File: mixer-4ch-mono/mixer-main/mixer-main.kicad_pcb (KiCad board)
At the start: 2 copper layers, 35 parts, among them J1 USB_C_Receptacle_PowerOnly_6P, J2 Conn_01x02, J3 Conn_01x02, J4 Conn_01x02, J5 Conn_01x02, J6 Conn_01x02, U1 TLV9062IDR, U2 TLV431AIDBZR, U3 SPX3819M5-L-3-3

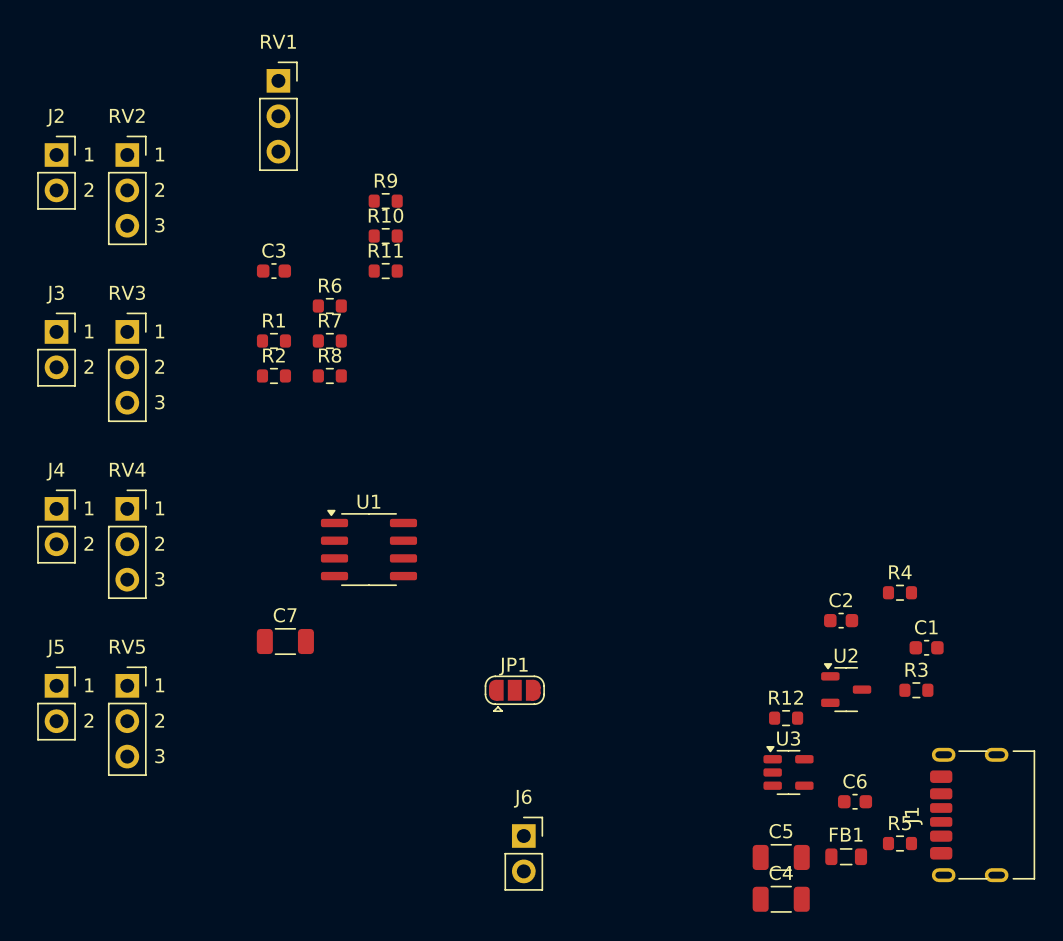
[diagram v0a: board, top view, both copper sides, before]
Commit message: Update mixer-main
Continued with layout.
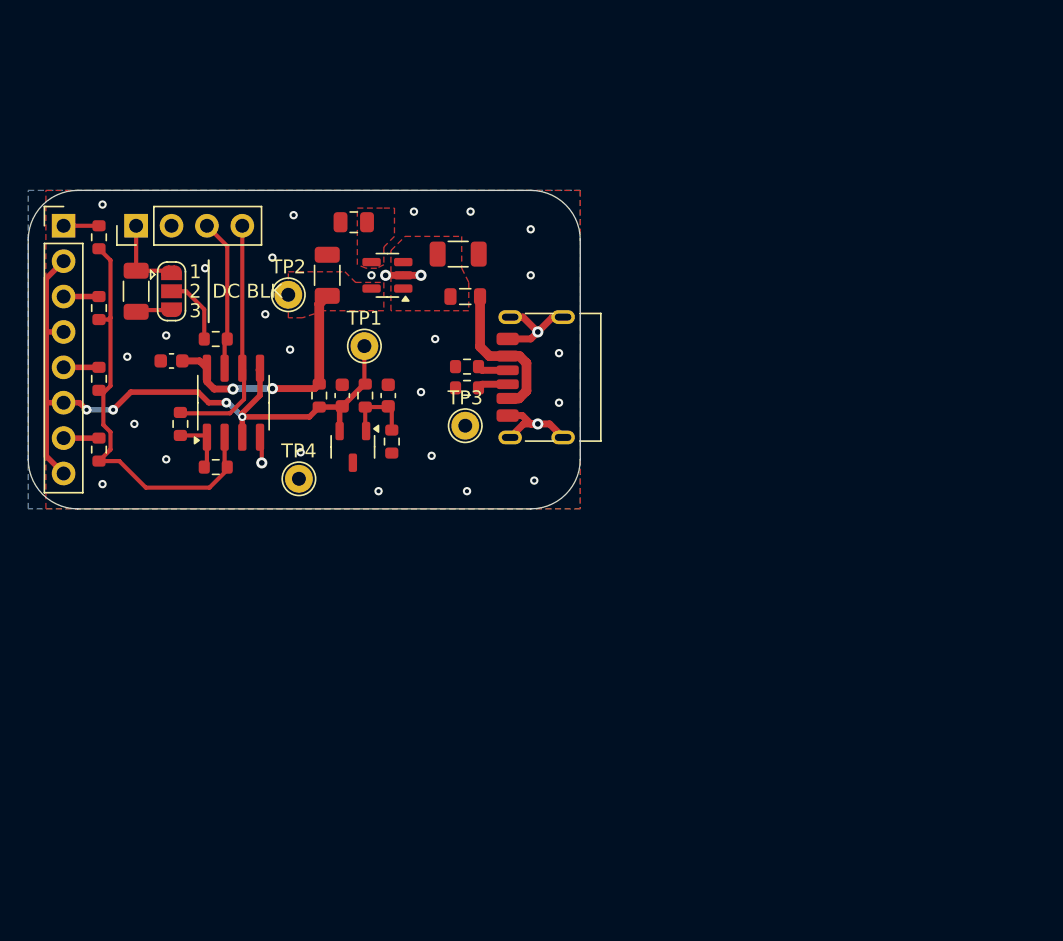
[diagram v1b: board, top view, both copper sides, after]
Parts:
- removed J4, J5, J6: Conn_01x02, Connector_PinSocket_2.54mm:PinSocket_1x02_P2.54mm_Vertical
- removed RV1: A/B10k, Connector_PinSocket_2.54mm:PinSocket_1x03_P2.54mm_Vertical
- removed RV2, RV3, RV4, RV5: 10k, Connector_PinSocket_2.54mm:PinSocket_1x03_P2.54mm_Vertical
- added TP1: VREF, TestPoint:TestPoint_THTPad_D2.0mm_Drill1.0mm, F.Cu at (146.6, 82.3)
- added TP2: 3.3V, TestPoint:TestPoint_THTPad_D2.0mm_Drill1.0mm, F.Cu at (141.1, 78.6)
- added TP3: VBUS, TestPoint:TestPoint_THTPad_D2.0mm_Drill1.0mm, F.Cu at (153.8, 88.0)
- added TP4: MIX_NODE, TestPoint:TestPoint_THTPad_D2.0mm_Drill1.0mm, F.Cu at (141.9, 91.8)
- C6: footprint Capacitor_SMD:C_0603_1608Metric -> Capacitor_SMD:C_0805_2012Metric
- J2: value Conn_01x02 -> HEADER_OUT; footprint Connector_PinSocket_2.54mm:PinSocket_1x02_P2.54mm_Vertical -> Connector_PinHeader_2.54mm:PinHeader_1x04_P2.54mm_Vertical
- J3: value Conn_01x02 -> Conn_01x08; footprint Connector_PinSocket_2.54mm:PinSocket_1x02_P2.54mm_Vertical -> Connector_PinHeader_2.54mm:PinHeader_1x08_P2.54mm_Vertical
- moved C6 55.0 mm to (145.8, 73.4), turned to 180 degrees
- moved C5 53.0 mm to (143.9, 77.2), turned to 90 degrees
- moved C4 51.8 mm to (153.3, 75.7)
- moved FB1 48.6 mm to (153.8, 78.7), turned to 180 degrees
- moved U3 45.9 mm to (148.2, 77.2), turned to 180 degrees
- moved C1 45.7 mm to (145.0, 85.8), turned to 90 degrees
- moved R5 45.1 mm to (153.9, 85.3), turned to 180 degrees
- moved J1 44.2 mm to (160.0, 84.5)
- moved R3 41.7 mm to (148.5, 89.1), turned to -90 degrees
- moved R4 40.9 mm to (146.6, 85.8), turned to -90 degrees
- moved R12 40.7 mm to (143.3, 85.8), turned to -90 degrees
- moved U2 39.5 mm to (145.7, 89.5), turned to -90 degrees
- moved JP1 37.8 mm to (132.7, 78.4), turned to -90 degrees
- moved C2 36.3 mm to (148.3, 85.8), turned to 90 degrees
- moved C7 27.3 mm to (130.2, 78.4), turned to -90 degrees
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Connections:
- net Net-(U3-BP) renamed /LDO_FB
- net Net-(U3-EN) renamed /LDO_IN
- C7 pad 1: Net-(J6-Pin_1) -> /MIX_OUT
- J2 pad 1: Net-(J2-Pin_1) -> /MIX_OUT
- J2 pad 2: /VREF_1.65V -> GND
- J3 pad 1: Net-(J3-Pin_1) -> /IN_SIG_1
- JP1 pad 1: Net-(J6-Pin_1) -> /MIX_OUT
- R10 pad 1: Net-(R10-Pad1) -> /IN_SIG_4
- R11 pad 1: Net-(R11-Pad1) -> /TO_OPAMP_7
- R2 pad 2: Net-(U1B--) -> /TO_OPAMP_6
- R7 pad 1: Net-(R7-Pad1) -> /IN_SIG_1
- R8 pad 1: Net-(R8-Pad1) -> /IN_SIG_2
- R9 pad 1: Net-(R9-Pad1) -> /IN_SIG_3
- U1 pad 6: Net-(U1B--) -> /TO_OPAMP_6
- U1 pad 7: Net-(R11-Pad1) -> /TO_OPAMP_7
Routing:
- net /VREF_1.65V: track 0.00 -> 53.4 mm, vias 0 -> 4
- net Net-(U1A--): track 0.00 -> 30.2 mm
- net GND: track 0.00 -> 18.5 mm, vias 0 -> 30
- net +3.3V: track 0.00 -> 17.9 mm, vias 0 -> 2
- net /TO_OPAMP_6: track 0.00 -> 17.5 mm
- net Net-(FB1-Pad1): track 0.00 -> 11.0 mm
- net /TO_OPAMP_7: track 0.00 -> 10.9 mm
- net /MIX_OUT: track 0.00 -> 5.82 mm
- net Net-(U2-REF): track 0.00 -> 5.22 mm
- net Net-(JP1-C): track 0.00 -> 5.02 mm
- net Net-(R1-Pad2): track 0.00 -> 4.18 mm
- net /IN_SIG_1: track 0.00 -> 2.73 mm
- net Net-(JP1-B): track 0.00 -> 2.59 mm
- net /IN_SIG_4: track 0.00 -> 2.54 mm
- net /IN_SIG_3: track 0.00 -> 2.54 mm
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- added copper zone on F.Cu, net +3.3V
- added copper zone on F.Cu, net /LDO_FB
- added copper zone on F.Cu, net /LDO_IN
- added copper zone on B.Cu, net GND
- added copper zone on F.Cu, net GND
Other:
- board outline added: 39.6 x 22.9 mm
- rule pad_to_mask_clearance: 0 -> 0.038
- board text added: "2.2uF"
- board text added: "DC BLK"

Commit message: Finalize mixer-4ch-mono rev. A
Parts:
- moved J2 1.27 mm to (131.4, 73.7)
- moved TP3 1.14 mm to (153.8, 89.2)
- moved TP4 0.46 mm to (141.6, 91.4)
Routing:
- net Net-(U1A--): track 30.2 -> 35.5 mm
- net Net-(FB1-Pad1): track 11.0 -> 16.1 mm
- net /TO_OPAMP_6: track 17.5 -> 18.0 mm
- net /TO_OPAMP_7: track 10.9 -> 10.4 mm
- net /MIX_OUT: track 5.82 -> 6.34 mm
- net GND: track 18.5 -> 18.0 mm, vias 30 -> 33
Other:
- board text added: "3v3"
- board text added: "blk"
- board text added: "dc"
- board text added: "gnd"
- board text added: "in 1"
- board text added: "in 2"
- board text added: "in 3"
- board text added: "in 4"
- board text added: "mix"
- board text added: "mixer-4ch-mono"
- board text added: "op6"
- board text added: "op7"
- board text added: "out"
- board text added: "patch_bits"
- board text added: "rev A"
- board text added: "vbus"
- board text added: "vref"
- board text removed: "DC BLK"
